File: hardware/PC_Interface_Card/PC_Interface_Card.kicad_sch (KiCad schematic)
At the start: 0 parts

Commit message: Updated final schematic, BoM and footprint assignment, imported schema to PCB
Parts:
- added C1, C10, C14, C5: 1u_16V_0603, Capacitor_SMD:C_0603_1608Metric, symbol Device:C
- added C11, C12, C13, C15, C16, C17, C18, C2, C3, C4, C6, C7, C8, C9: 100n_16V_0603, Capacitor_SMD:C_0603_1608Metric, symbol Device:C
- added CR1: SS14, Footprint_Project_PC_Interface:SS14_CR_SMA_403AE_OSI-M, symbol SS14_2026-01-11_07-18-03:SS14
- added F1: C1Q 1.5, Footprint:C1_BEL-M, symbol BEL_C1_2026-01-11_07-01-53:C1Q_1.5
- added FL1: BLM18PG600SN1D, Footprint:BEAD_BLM18PG_C1608X95N, symbol BLM18PG600SN1D:BLM18PG600SN1D
- added J1: GSB1C41110SSHR, Footprint:AMPHENOL_GSB1C41110SSHR, symbol GSB1C41110SSHR:GSB1C41110SSHR
- added J2: Conn_01x10_Pin, Connector_PinSocket_1.00mm:PinSocket_1x10_P1.00mm_Vertical, symbol Connector:Conn_01x10_Pin
- added J3: DM3BT-DSF-PEJS, Footprint_Project_PC_Interface:HRS_DM3BT-DSF-PEJS, symbol DM3BT-DSF-PEJS:DM3BT-DSF-PEJS
- added Q1: PMOS, Package_TO_SOT_SMD:SOT-23-3, symbol Simulation_SPICE:PMOS
- added R1, R11, R12, R15, R17, R18, R19, R22, R23, R25, R26, R27, R28, R29, R3, R31, R32, R4, R5, R6, R7, R8: 10k_0.2W_0603, Resistor_SMD:R_0603_1608Metric, symbol Device:R
- added R10, R9: 5.1k_0.2W_0603, Resistor_SMD:R_0603_1608Metric, symbol Device:R
- added R13, R14, R16, R20, R21, R24, R30: 68R_0.2W_0603, Resistor_SMD:R_0603_1608Metric, symbol Device:R
- added R2: 4R7_0.2W_0603, Resistor_SMD:R_0603_1608Metric, symbol Device:R
- added S1: PEC11R-4120K-S0018, Footprint:XDCR_PEC11R-4120K-S0018, symbol PEC11R-4120K-S0018:PEC11R-4120K-S0018
- added SW1, SW2, SW3, SW4, SW5: B3W-900-1, Footprint:B3W-900-1_OMR, symbol B3W_9000_2026-01-10_20-59-16:B3W-900-1
- added SW6, SW7: TL1240YQ2JBLK, Footprint:TL1240YQ, symbol Custom_Switch_LED:TL1240YQ2JBLK
- added U1: USBLC6-2SC6, Package_TO_SOT_SMD:SOT-23-6, symbol Power_Protection:USBLC6-2SC6
- added U2: TLV1117LV33DCYR, Footprint:VREG_TLV1117LV33DCYR, symbol TLV1117LV33DCYR:TLV1117LV33DCYR
- added U3: MB85RS4MTYPN-GS-AWEWE1, Footprint:DFN8_FUJ-M, symbol 2026-01-10_16-38-32:MB85RS4MTYPN-GS-AWEWE1
- added U4: ESP32-S3-WROOM-1, RF_Module:ESP32-S3-WROOM-1, symbol RF_Module:ESP32-S3-WROOM-1
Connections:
- new net: Q1.1 (D), R2.2
- new net: R14.1, SW2.5 (ANODE)
- new net: R30.1, SW7.5 (+)
- new net: R26.2, U4.15 (IO3)
- new net: R31.2, U4.16 (IO46)
- new net: R32.2, U4.26 (IO45)
- new net: R17.1, U3.3 (*WP)
- new net: CR1.2, FL1.2
- new net: R20.1, SW4.5 (ANODE)
- new net: R16.1, SW3.5 (ANODE)
- new net: R13.1, SW1.5 (ANODE)
- new net: R24.1, SW6.5 (+)
- new net: R22.2, U3.7 (*RESET)
- new net: F1.2, FL1.1
- new net: R21.1, SW5.5 (ANODE)
- new net CC1: J1.A5 (CC1), R9.1
- new net CC2: J1.B5 (CC2), R10.1
- new net CLK_SDMMC: J3.5 (CLK), U4.32 (IO39)
- new net CMD_SDMMC: J3.3 (CMD), R7.1, U4.31 (IO38)
- new net CS_DISP: J2.3 (Pin_3), U4.18 (IO10)
- new net D+: J1.A6 (DP1), U1.1 (I/O1), U1.6 (I/O1), U4.14 (USB_D+)
- new net D-: J1.A7 (DN1), U1.3 (I/O2), U1.4 (I/O2), U4.13 (USB_D-)
- new net D0_SDMMC: J3.7 (DAT0), R1.1, U4.33 (IO40)
- new net D1_SDMMC: J3.8 (DAT1), R3.1, U4.34 (IO41)
- new net D2_SDMMC: J3.1 (DAT2), R4.1, U4.35 (IO42)
- new net D3_SDMMC: J3.2 (DAT3/CD), R5.1, U4.24 (IO47)
- new net DC_DISP: J2.2 (Pin_2), U4.17 (IO9)
- new net ENC_A: C17.1, R27.1, S1.A, U4.4 (IO4)
- new net ENC_B: C18.1, R29.1, S1.B, U4.5 (IO5)
- new net ENC_SW: C13.1, R25.1, S1.1, U4.6 (IO6)
- new net FRAM_CS: U3.1 (*CS), U4.22 (IO14)
- new net GND: C1.2, C10.2, C11.2, C12.2, C13.2, C14.2, C15.2, C16.2, C17.2, C18.2, C2.2, C3.2, C4.2, C5.2, C6.2, C7.2, C8.2, C9.2, J1.A1_B12 (GND_A), J1.B1_A12 (GND_B), J1.SH1 (SHIELD), J1.SH2 (SHIELD__1), J1.SH3 (SHIELD__2), J1.SH4 (SHIELD__3), J2.9 (Pin_9), J3.6 (VSS), J3.S1 (SHIELD), J3.S2 (SHIELD__1), J3.S3 (SHIELD__2), J3.S4 (SHIELD__3), R10.2, R22.1, R26.1, R31.1, R32.1, R6.1, R9.2, S1.2, S1.C (COM), S1.SH1 (SHIELD), S1.SH2 (SHIELD__1), SW1.3, SW1.4, SW1.6 (CATHODE), SW2.3, SW2.4, SW2.6 (CATHODE), SW3.3, SW3.4, SW3.6 (CATHODE), SW4.3, SW4.4, SW4.6 (CATHODE), SW5.3, SW5.4, SW5.6 (CATHODE), SW6.3, SW6.4, SW6.6 (-), SW7.3, SW7.4, SW7.6 (-), U1.2 (GND), U2.1 (GND), U3.4 (VSS), U3.9 (VSS), U4.1 (GND), U4.40 (GND), U4.41 (GND)
- new net LED_DISP: J2.8 (Pin_8), R2.1
- new net MISO: J2.6 (Pin_6), U3.2 (SO), U4.21 (IO13)
- new net MOSI: J2.4 (Pin_4), U3.5 (SI), U4.19 (IO11)
- new net PWM_DISP: Q1.2 (G), R6.2, U4.25 (IO48)
- new net RST_DISP: J2.7 (Pin_7), R8.1, U4.12 (IO8)
- new net SCLK: J2.5 (Pin_5), U3.6 (SCK), U4.20 (IO12)
- new net SW_BOOT: C16.1, R28.1, SW7.1, SW7.2, U4.27 (IO0)
- new net SW_DN: C9.1, R19.1, SW5.1, SW5.2, U4.11 (IO18)
- new net SW_EN: C12.1, R23.1, SW6.1, SW6.2, U4.3 (EN)
- new net SW_LEFT: C3.1, R11.1, SW1.1, SW1.2, U4.10 (IO17)
- new net SW_MENU: C7.1, R15.1, SW3.1, SW3.2, U4.8 (IO15)
- new net SW_RIGHT: C8.1, R18.1, SW4.1, SW4.2, U4.37 (TXD0)
- new net SW_UP: C4.1, R12.1, SW2.1, SW2.2, U4.9 (IO16)
- new net VCC: C1.1, C10.1, C11.1, C14.1, C15.1, C2.1, J2.1 (Pin_1), J3.4 (VDD), Q1.3 (S), R1.2, R11.2, R12.2, R13.2, R14.2, R15.2, R16.2, R17.2, R18.2, R19.2, R20.2, R21.2, R23.2, R24.2, R25.2, R27.2, R28.2, R29.2, R3.2, R30.2, R4.2, R5.2, R7.2, R8.2, U2.2 (OUT_2), U2.4 (OUT_4), U3.8 (VDD), U4.2 (3V3)
- new net VLDO: C5.1, C6.1, CR1.1, U2.3 (IN)
- new net VUSB: F1.1, J1.A4_B9 (VBUS_A), J1.B4_A9 (VBUS_B), U1.5 (VBUS)
- no-connect marks 0 -> 15
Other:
- note added: "Controller"
- note added: "Display Connector"
- note added: "EN/BOOT Switches"
- note added: "Encoder"
- note added: "FRAM"
- note added: "LDO"
- note added: "Navigation Switches"
- note added: "SDMMC Connector"
- note added: "USB Prot Diode"
- note added: "USB Protection and Config"
- note added: "USB Receptacle"

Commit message: footprint and 3d model fixes, footprint mismatch persists for B3W-9000 still. Need a fix.
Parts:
- SW1, SW2, SW3, SW4, SW5: footprint Footprint:B3W-900-1_OMR -> Footprint:SW6_B3W-9-1_OMR
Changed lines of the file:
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@@
 			)
 		)
-		(property "Footprint" "Footprint:B3W-900-1_OMR"
+		(property "Footprint" "Footprint:SW6_B3W-9-1_OMR"
 			(at 273.05 124.46 0)
 			(effects
@@
 			)
 		)
-		(property "Footprint" "Footprint:B3W-900-1_OMR"
+		(property "Footprint" "Footprint:SW6_B3W-9-1_OMR"
 			(at 194.31 172.72 0)
 			(effects
@@
 			)
 		)
-		(property "Footprint" "Footprint:B3W-900-1_OMR"
+		(property "Footprint" "Footprint:SW6_B3W-9-1_OMR"
 			(at 194.31 125.73 0)
 			(effects
@@
 			)
 		)
-		(property "Footprint" "Footprint:B3W-900-1_OMR"
+		(property "Footprint" "Footprint:SW6_B3W-9-1_OMR"
 			(at 237.49 219.71 0)
 			(effects
@@
 			)
 		)
-		(property "Footprint" "Footprint:B3W-900-1_OMR"
+		(property "Footprint" "Footprint:SW6_B3W-9-1_OMR"
 			(at 273.05 172.72 0)
 			(effects

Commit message: Schematic changes
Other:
- note added: "OakBridge MkI"
- moved on the sheet: C1, C10, C11, C12, C13, C14, C15, C16, C17, C18, C2, C3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

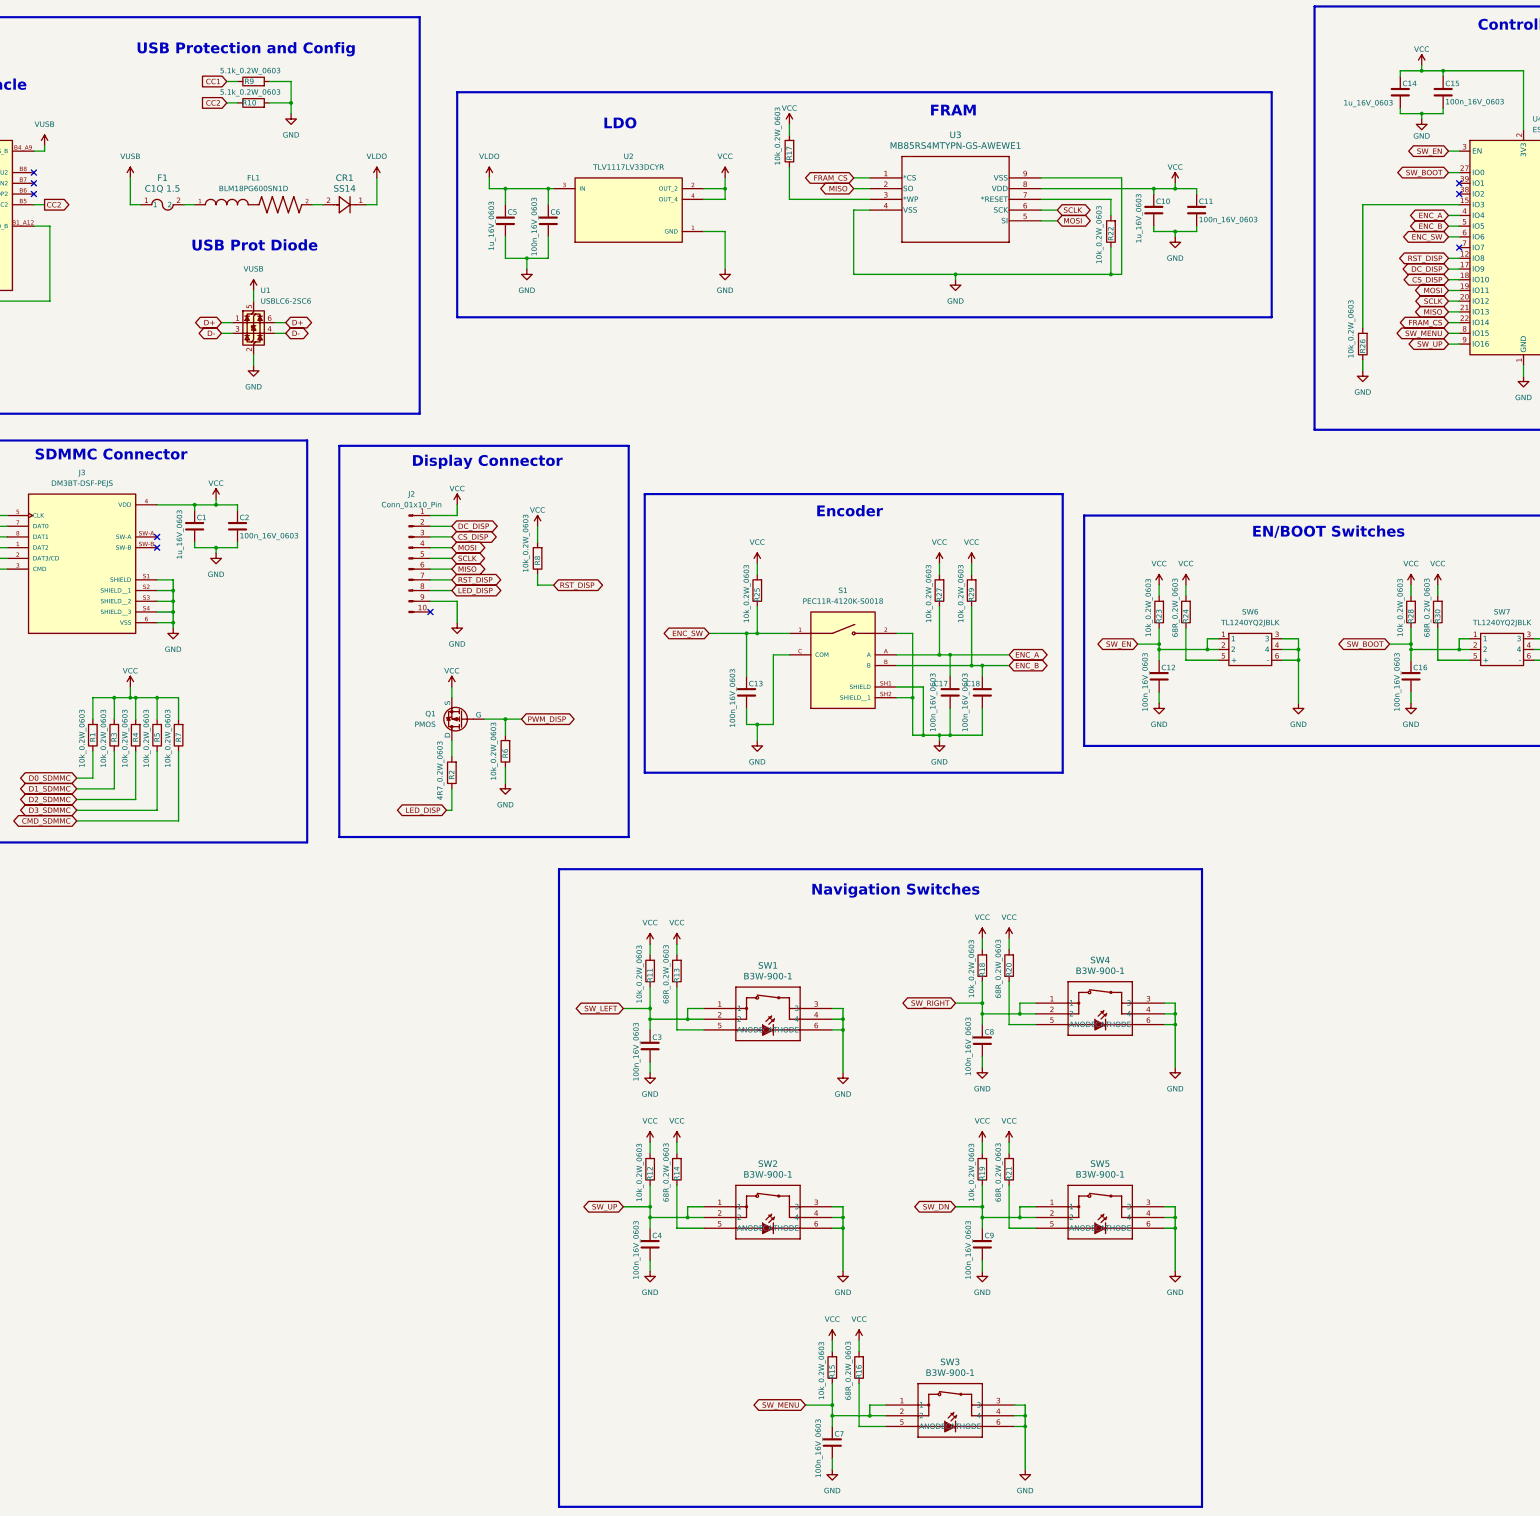
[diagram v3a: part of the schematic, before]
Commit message: Footprints added with BoM update and all 3d models added.
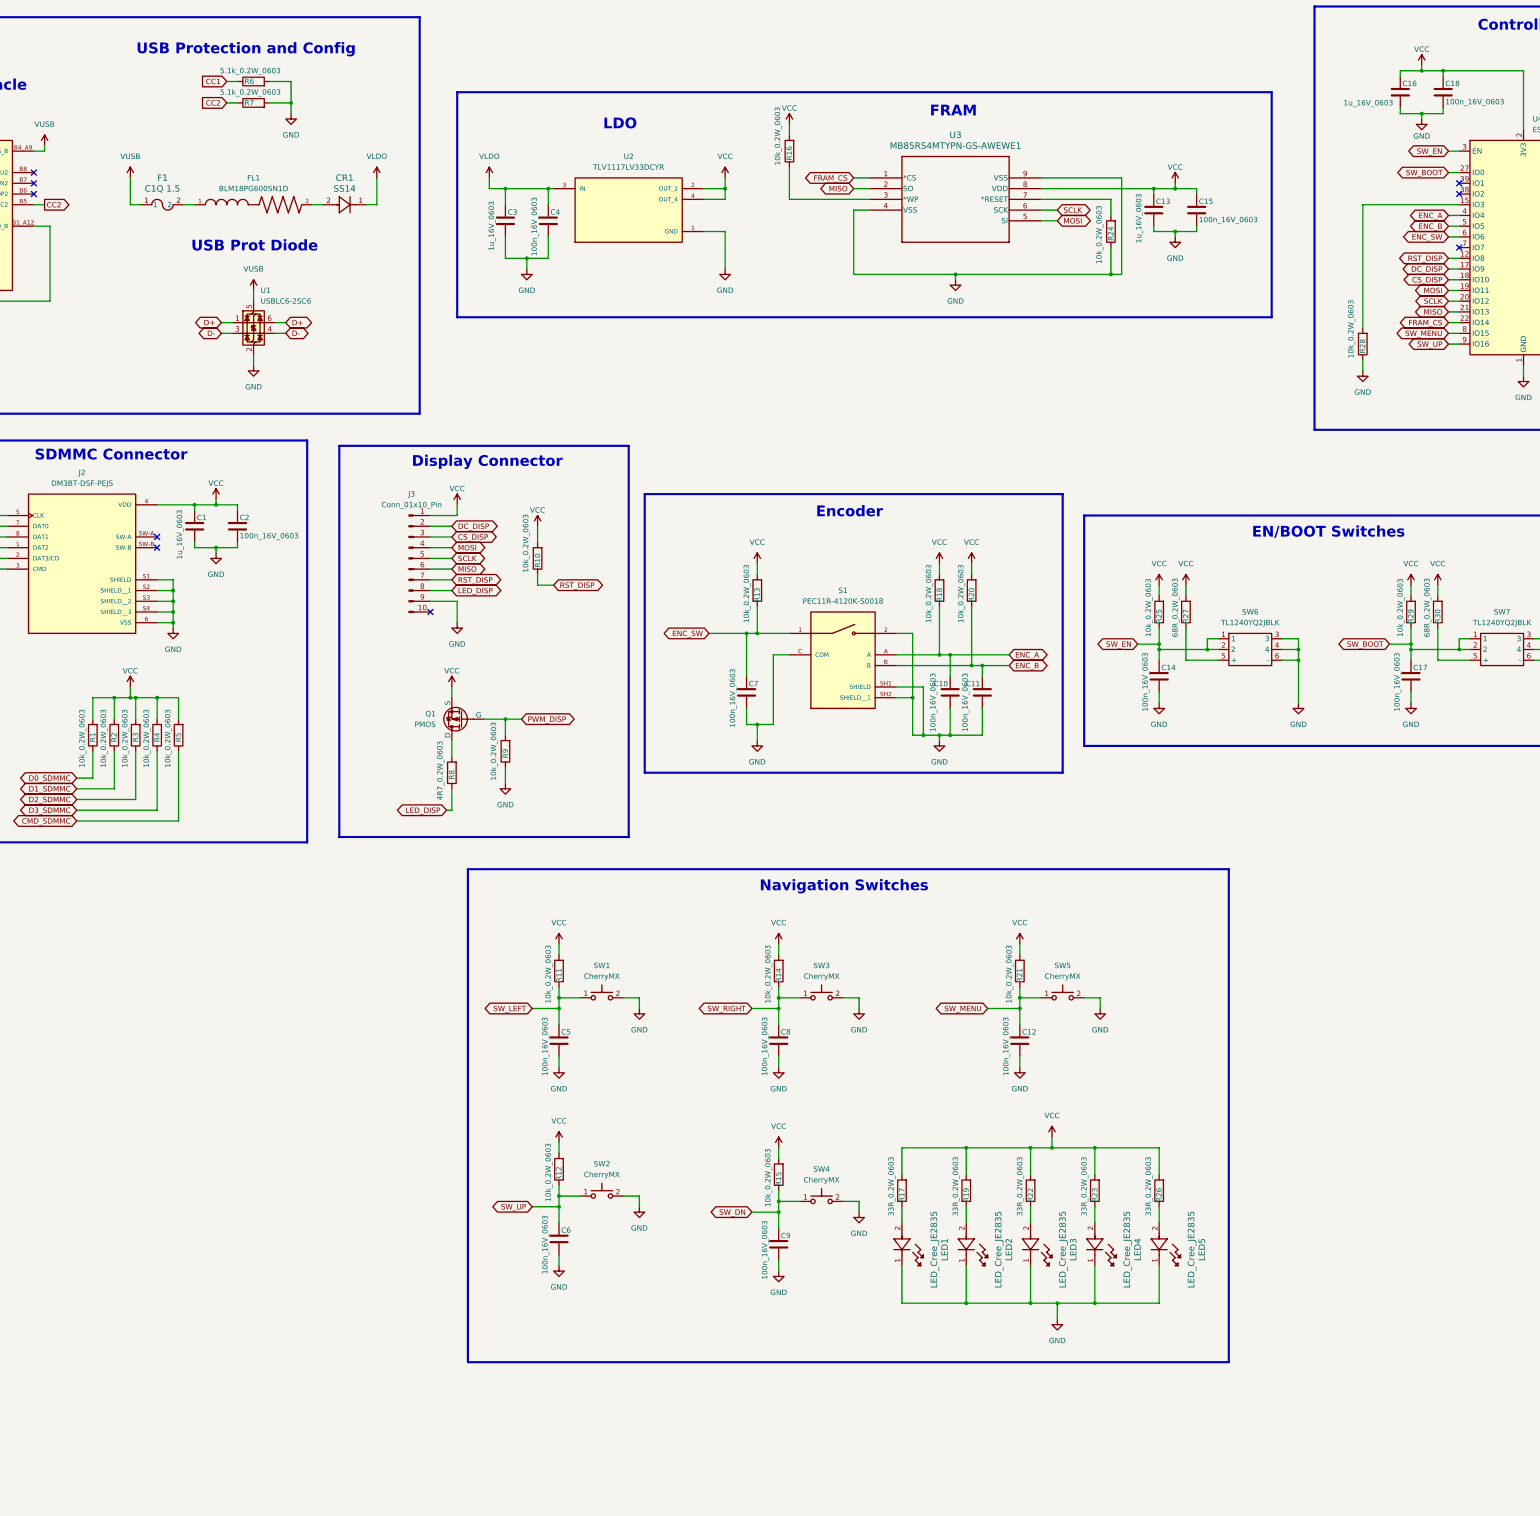
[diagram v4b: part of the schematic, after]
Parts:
- removed C4, C7: 100n_16V_0603, Capacitor_SMD:C_0603_1608Metric, symbol Device:C
- removed R13, R16, R20: 68R_0.2W_0603, Resistor_SMD:R_0603_1608Metric, symbol Device:R
- removed R18: 10k_0.2W_0603, Resistor_SMD:R_0603_1608Metric, symbol Device:R
- removed SW1, SW2, SW3, SW4, SW5: B3W-900-1, Footprint:SW6_B3W-9-1_OMR, symbol B3W_9000_2026-01-10_20-59-16:B3W-900-1
- added C12, C6: 100n_16V_0603, Capacitor_SMD:C_0603_1608Metric, symbol Device:C
- added LED1, LED2, LED3, LED4, LED5: LED_Cree_JE2835, Footprint:LED_JE2835_CRW-M, symbol LED_PC_Interface:JE2835ARY-N-0002A0000-N0000001
- added R17, R22, R23, R26: 33R_0.2W_0603, Resistor_SMD:R_0603_1608Metric, symbol Device:R
- added SW1, SW2, SW3, SW4, SW5: CherryMX, CherryMX_PCB:CherryMX_1.00u_PCB, symbol CherryMX:CherryMX
- R14, R21: value 68R_0.2W_0603 -> 10k_0.2W_0603; Manufacturer YAGEO -> Panasonic Electronic Components; Manufacturer Part Number RC0603FR-7W68RL -> ERJ-PB3B1002V; Vendor Link https://www.digikey.in/en/products/detail/yageo/RC0603FR-7W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 -> https://www.digikey.in/en/products/detail/panasonic-electro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; Vendor Part Number 13-RC0603FR-7W68RLCT-ND -> P20086CT-ND
- R19: value 10k_0.2W_0603 -> 33R_0.2W_0603; Manufacturer Panasonic Electronic Components -> TE Connectivity Passive Product; Manufacturer Part Number ERJ-PB3B1002V -> CRGH0603J33R; Vendor Link https://www.digikey.in/en/products/detail/panasonic-electro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 -> https://www.digikey.in/en/products/detail/te-connectivity-p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; Vendor Part Number P20086CT-ND -> 1712-CRGH0603J33RCT-ND
- renumbered C17 to C10, C18 to C11, C10 to C13, C12 to C14, C11 to C15, C14 to C16, C16 to C17, C15 to C18, C5 to C3, C6 to C4, C3 to C5, C13 to C7, J3 to J2, J2 to J3, R8 to R10, R25 to R13, R17 to R16, R27 to R18, R3 to R2, R29 to R20, R22 to R24, R23 to R25, R24 to R27, R26 to R28, R28 to R29, R4 to R3, R5 to R4, R7 to R5, R9 to R6, R10 to R7, R2 to R8, R6 to R9
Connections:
- net GND: now also C12.2, C6.2, LED1.1, LED2.1, LED3.1, LED4.1, LED5.1, SW1.2, SW2.2, SW3.2, SW4.2, SW5.2
- net SW_DN: now also R15.1, SW4.1; no longer R19.1
- net SW_LEFT: now also SW1.1
- net SW_MENU: now also R21.1, C12.1, SW5.1; no longer R15.1
- net SW_RIGHT: now also R14.1, SW3.1
- net SW_UP: now also C6.1, SW2.1
- net VCC: now also R17.2, R22.2, R23.2, R26.2
- new net: LED4.2, R23.1
- new net: LED1.2, R17.1
- new net: LED2.2, R19.1
- new net: LED3.2, R22.1
- new net: LED5.2, R26.1
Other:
- title: PC Interface Card -> OakBridge MkI
- moved on the sheet: C5, R11
